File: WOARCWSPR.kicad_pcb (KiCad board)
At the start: 2 copper layers, 65 x 30.5 mm, 27 parts, among them J1 TP2, J2 Raspberry_Pi_2_3, J3 TP2, J4 Conn_Coaxial, J5 LPF_OUT, J6 LPF_IN, J7 TP1, J8 TP2, Q1 BS170, SW1 SW_Push_Dual

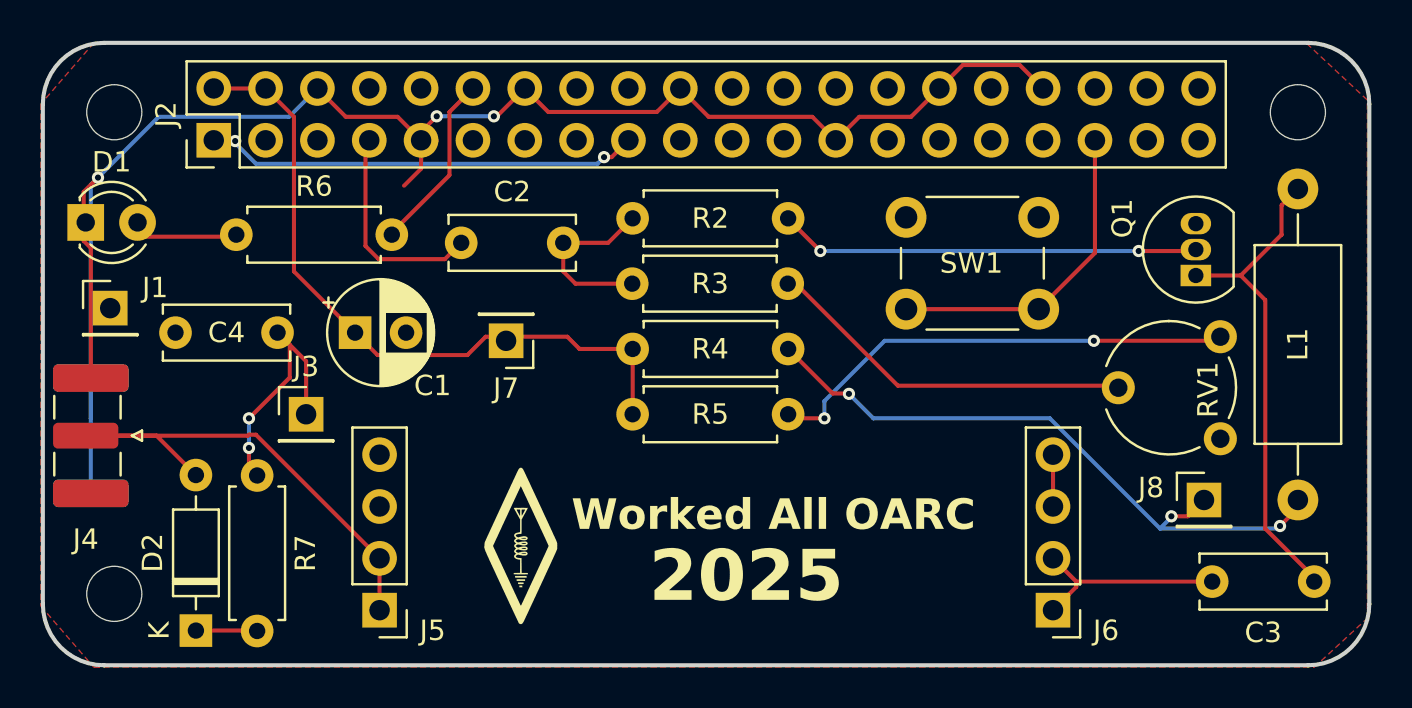
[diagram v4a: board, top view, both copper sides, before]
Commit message: Make J7 routing prettier
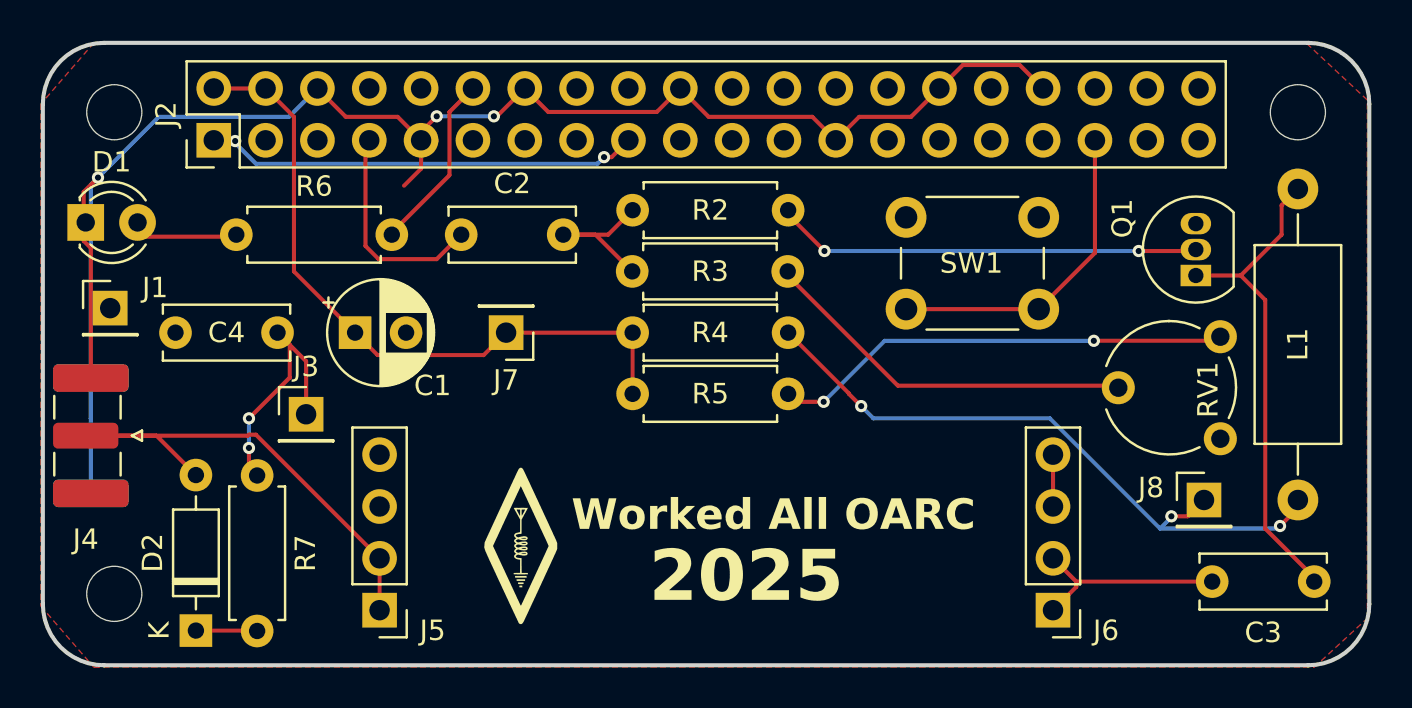
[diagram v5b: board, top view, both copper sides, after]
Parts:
- moved R5 1.00 mm to (188.4, 47.2)
- moved R4 0.80 mm to (188.4, 44.2)
- moved R3 0.60 mm to (196.0, 41.2)
- moved C2 0.40 mm to (180.0, 39.4)
- moved J7 0.40 mm to (182.2, 44.2)
- moved R2 0.40 mm to (188.4, 38.2)
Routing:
- net Net-(C2-Pad2): track 8.93 -> 8.02 mm
- net Net-(R5-Pad2): track 23.4 -> 22.7 mm
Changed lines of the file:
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@@
 	(footprint "Capacitor_THT:C_Disc_D6.0mm_W2.5mm_P5.00mm"
 		(layer "F.Cu")
-		(at 180 39.8)
+		(at 180 39.4)
 		(descr "C, Disc series, Radial, pin pitch=5.00mm, , diameter*width=6*2.5mm^2, Capacitor, http://cdn-reichelt.de/documents/datenblatt/B300/DS_KERKO_TC.pdf")
 		(tags "C Disc series Radial pin pitch 5.00mm  diameter 6mm width 2.5mm Capacitor")
@@
 	(footprint "Resistor_THT:R_Axial_DIN0207_L6.3mm_D2.5mm_P7.62mm_Horizontal"
 		(layer "F.Cu")
-		(at 188.4 38.6)
+		(at 188.4 38.2)
 		(descr "Resistor, Axial_DIN0207 series, Axial, Horizontal, pin pitch=7.62mm, 0.25W = 1/4W, length*diameter=6.3*2.5mm^2, http://cdn-reichelt.de/documents/datenblatt/B400/1_4W%23YAG.pdf")
 		(tags "Resistor Axial_DIN0207 series Axial Horizontal pin pitch 7.62mm 0.25W = 1/4W length 6.3mm diameter 2.5mm")
@@
 	(footprint "Connector_PinHeader_2.54mm:PinHeader_1x01_P2.54mm_Vertical"
 		(layer "F.Cu")
-		(at 182.2 44.6 180)
+		(at 182.2 44.2 180)
 		(descr "Through hole straight pin header, 1x01, 2.54mm pitch, single row")
 		(tags "Through hole pin header THT 1x01 2.54mm single row")
@@
 	(footprint "Resistor_THT:R_Axial_DIN0207_L6.3mm_D2.5mm_P7.62mm_Horizontal"
 		(layer "F.Cu")
-		(at 196 41.8 180)
+		(at 196 41.2 180)
 		(descr "Resistor, Axial_DIN0207 series, Axial, Horizontal, pin pitch=7.62mm, 0.25W = 1/4W, length*diameter=6.3*2.5mm^2, http://cdn-reichelt.de/documents/datenblatt/B400/1_4W%23YAG.pdf")
 		(tags "Resistor Axial_DIN0207 series Axial Horizontal pin pitch 7.62mm 0.25W = 1/4W length 6.3mm diameter 2.5mm")
@@
 	(footprint "Resistor_THT:R_Axial_DIN0207_L6.3mm_D2.5mm_P7.62mm_Horizontal"
 		(layer "F.Cu")
-		(at 188.4 45)
+		(at 188.4 44.2)
 		(descr "Resistor, Axial_DIN0207 series, Axial, Horizontal, pin pitch=7.62mm, 0.25W = 1/4W, length*diameter=6.3*2.5mm^2, http://cdn-reichelt.de/documents/datenblatt/B400/1_4W%23YAG.pdf")
 		(tags "Resistor Axial_DIN0207 series Axial Horizontal pin pitch 7.62mm 0.25W = 1/4W length 6.3mm diameter 2.5mm")
@@
 	(footprint "Resistor_THT:R_Axial_DIN0207_L6.3mm_D2.5mm_P7.62mm_Horizontal"
 		(layer "F.Cu")
-		(at 188.4 48.2)
+		(at 188.4 47.2)
 		(descr "Resistor, Axial_DIN0207 series, Axial, Horizontal, pin pitch=7.62mm, 0.25W = 1/4W, length*diameter=6.3*2.5mm^2, http://cdn-reichelt.de/documents/datenblatt/B400/1_4W%23YAG.pdf")
 		(tags "Resistor Axial_DIN0207 series Axial Horizontal pin pitch 7.62mm 0.25W = 1/4W length 6.3mm diameter 2.5mm")
@@
 	)
 	(segment
-		(start 187.2 39.8)
-		(end 188.4 38.6)
+		(start 187.2 39.4)
+		(end 185 39.4)
 		(width 0.2)
 		(layer "F.Cu")
@@
 	)
 	(segment
-		(start 185.6 41.8)
-		(end 185 41.2)
+		(start 188.38 41.2)
+		(end 186.58 39.4)
 		(width 0.2)
 		(layer "F.Cu")
@@
 	)
 	(segment
-		(start 187.2 39.8)
-		(end 185 39.8)
+		(start 188.4 38.2)
+		(end 187.2 39.4)
 		(width 0.2)
 		(layer "F.Cu")
@@
 	)
 	(segment
-		(start 185 41.2)
-		(end 185 39.8)
+		(start 186.58 39.4)
+		(end 185 39.4)
 		(width 0.2)
 		(layer "F.Cu")
@@
 	)
 	(segment
-		(start 185.6 41.8)
-		(end 188.38 41.8)
-		(width 0.2)
-		(layer "F.Cu")
-		(net 2)
-	)
-	(segment
-		(start 175.495 34.775)
-		(end 175.495 34.895)
+		(start 178.8 40.6)
+		(end 180 39.4)
 		(width 0.2)
 		(layer "F.Cu")
@@
 	)
 	(segment
-		(start 179.2 40.6)
-		(end 180 39.8)
+		(start 175.31 39.955635)
+		(end 175.954365 40.6)
 		(width 0.2)
 		(layer "F.Cu")
@@
 	)
 	(segment
-		(start 175.6 35)
-		(end 175.31 35.29)
+		(start 175.31 35.29)
+		(end 175.31 39.955635)
 		(width 0.2)
 		(layer "F.Cu")
@@
 	)
 	(segment
-		(start 175.31 35.29)
-		(end 175.31 39.955635)
+		(start 175.495 34.895)
+		(end 175.6 35)
 		(width 0.2)
 		(layer "F.Cu")
@@
 	)
 	(segment
-		(start 175.954365 40.6)
-		(end 179.2 40.6)
+		(start 175.6 35)
+		(end 175.31 35.29)
 		(width 0.2)
 		(layer "F.Cu")
@@
 	)
 	(segment
-		(start 175.31 39.955635)
-		(end 175.954365 40.6)
+		(start 175.495 34.775)
+		(end 175.495 34.895)
 		(width 0.2)
 		(layer "F.Cu")
@@
 	)
 	(segment
-		(start 175.495 34.895)
-		(end 175.6 35)
+		(start 175.954365 40.6)
+		(end 178.8 40.6)
 		(width 0.2)
 		(layer "F.Cu")
@@
 	)
 	(segment
-		(start 196.02 38.62)
-		(end 197.6 40.2)
+		(start 213.2 40.2)
+		(end 215.93 40.2)
 		(width 0.2)
 		(layer "F.Cu")
@@
 	)
 	(segment
-		(start 213.2 40.2)
-		(end 215.93 40.2)
+		(start 197.8 40.2)
+		(end 196.02 38.42)
 		(width 0.2)
 		(layer "F.Cu")
@@
 	)
 	(segment
-		(start 215.93 40.2)
-		(end 216 40.13)
+		(start 196.02 38.42)
+		(end 196.02 38.2)
 		(width 0.2)
 		(layer "F.Cu")
@@
 	)
 	(segment
-		(start 196.02 38.6)
-		(end 196.02 38.62)
+		(start 215.93 40.2)
+		(end 216 40.13)
 		(width 0.2)
 		(layer "F.Cu")
@@
 	)
 	(via
-		(at 197.6 40.2)
+		(at 197.8 40.2)
 		(size 0.6)
 		(drill 0.3)
@@
 	(segment
 		(start 213.2 40.2)
-		(end 197.6 40.2)
+		(end 197.8 40.2)
 		(width 0.2)
 		(layer "B.Cu")
@@
 	)
 	(segment
-		(start 185.2 44.4)
-		(end 185.8 45)
+		(start 188.4 44.2)
+		(end 182.2 44.2)
 		(width 0.2)
 		(layer "F.Cu")
@@
 	)
 	(segment
-		(start 181.2 44.4)
-		(end 185.2 44.4)
+		(start 175.9 45.3)
+		(end 181.1 45.3)
 		(width 0.2)
 		(layer "F.Cu")
@@
 	)
 	(segment
-		(start 175.9 45.3)
-		(end 174.8 44.2)
+		(start 174.8 44.2)
+		(end 175.9 45.3)
 		(width 0.2)
 		(layer "F.Cu")
@@
 	)
 	(segment
-		(start 181.2 44.4)
-		(end 180.3 45.3)
+		(start 188.4 47.2)
+		(end 188.4 44.2)
 		(width 0.2)
 		(layer "F.Cu")
@@
 	)
 	(segment
-		(start 185.8 45)
-		(end 188.4 45)
-		(width 0.2)
-		(layer "F.Cu")
-		(net 37)
-	)
-	(segment
-		(start 188.4 48.2)
-		(end 188.4 45)
-		(width 0.2)
-		(layer "F.Cu")
-		(net 37)
-	)
-	(segment
-		(start 180.3 45.3)
-		(end 175.9 45.3)
+		(start 181.1 45.3)
+		(end 182.2 44.2)
 		(width 0.2)
 		(layer "F.Cu")
@@
 	)
 	(segment
-		(start 199 47.2)
-		(end 198.979999 47.179999)
+		(start 198.999999 47.179999)
+		(end 196.02 44.2)
 		(width 0.2)
 		(layer "F.Cu")
@@
 	)
 	(segment
-		(start 198.979999 47.179999)
-		(end 198.199999 47.179999)
+		(start 215.6 53.2)
+		(end 216.4 52.4)
 		(width 0.2)
 		(layer "F.Cu")
@@
 	)
 	(segment
-		(start 215.6 53.2)
-		(end 216.4 52.4)
+		(start 221 52.8)
+		(end 221 52.4)
 		(width 0.2)
 		(layer "F.Cu")
@@
 	)
 	(segment
-		(start 221 52.8)
-		(end 221 52.4)
+		(start 198.999999 47.199999)
+		(end 198.999999 47.179999)
 		(width 0.2)
 		(layer "F.Cu")
@@
 	)
 	(segment
-		(start 198.199999 47.179999)
-		(end 196.02 45)
+		(start 220.124265 53.675735)
+		(end 221 52.8)
 		(width 0.2)
 		(layer "F.Cu")
@@
 	)
 	(segment
-		(start 220.124265 53.675735)
-		(end 221 52.8)
+		(start 199.6 47.8)
+		(end 198.999999 47.199999)
 		(width 0.2)
 		(layer "F.Cu")
@@
 	)
 	(via
-		(at 199 47.2)
+		(at 199.6 47.8)
 		(size 0.6)
 		(drill 0.3)
@@
 	)
 	(segment
-		(start 199 47.2)
+		(start 199.6 47.8)
 		(end 200.2 48.4)
 		(width 0.2)
@@
 	)
 	(segment
-		(start 200.2 48.4)
-		(end 208.846346 48.4)
+		(start 208.846346 48.4)
+		(end 214.246346 53.8)
 		(width 0.2)
 		(layer "B.Cu")
@@
 	)
 	(segment
-		(start 208.846346 48.4)
-		(end 214.246346 53.8)
+		(start 200.2 48.4)
+		(end 208.846346 48.4)
 		(width 0.2)
 		(layer "B.Cu")
@@
 	)
 	(segment
-		(start 196.4 41.8)
-		(end 201.4 46.8)
+		(start 212.1 46.8)
+		(end 212.2 46.9)
 		(width 0.2)
 		(layer "F.Cu")
@@
 	)
 	(segment
-		(start 201.4 46.8)
-		(end 212.1 46.8)
+		(start 196 41.4)
+		(end 201.4 46.8)
 		(width 0.2)
 		(layer "F.Cu")
@@
 	)
 	(segment
-		(start 196 41.8)
-		(end 196.4 41.8)
+		(start 201.4 46.8)
+		(end 212.1 46.8)
 		(width 0.2)
 		(layer "F.Cu")
@@
 	)
 	(segment
-		(start 212.1 46.8)
-		(end 212.2 46.9)
+		(start 196 41.2)
+		(end 196 41.4)
 		(width 0.2)
 		(layer "F.Cu")
@@
 	)
 	(segment
-		(start 196.02 48.2)
-		(end 196.22 48.4)
+		(start 217 44.6)
+		(end 217.2 44.4)
 		(width 0.2)
 		(layer "F.Cu")
@@
 	)
 	(segment
-		(start 217 44.6)
-		(end 217.2 44.4)
+		(start 197.761471 47.59)
+		(end 196.41 47.59)
 		(width 0.2)
 		(layer "F.Cu")
@@
 	)
 	(segment
-		(start 196.22 48.4)
-		(end 197.8 48.4)
+		(start 196.41 47.59)
+		(end 196.02 47.2)
 		(width 0.2)
 		(layer "F.Cu")
@@
 	)
 	(via
-		(at 197.8 48.4)
+		(at 197.761471 47.59)
 		(size 0.6)
 		(drill 0.3)
@@
 	)
 	(segment
-		(start 197.8 48.4)
-		(end 197.8 47.551471)
-		(width 0.2)
-		(layer "B.Cu")
-		(net 41)
-	)
-	(segment
-		(start 197.8 47.551471)
+		(start 197.761471 47.59)
 		(end 200.751471 44.6)
 		(width 0.2)

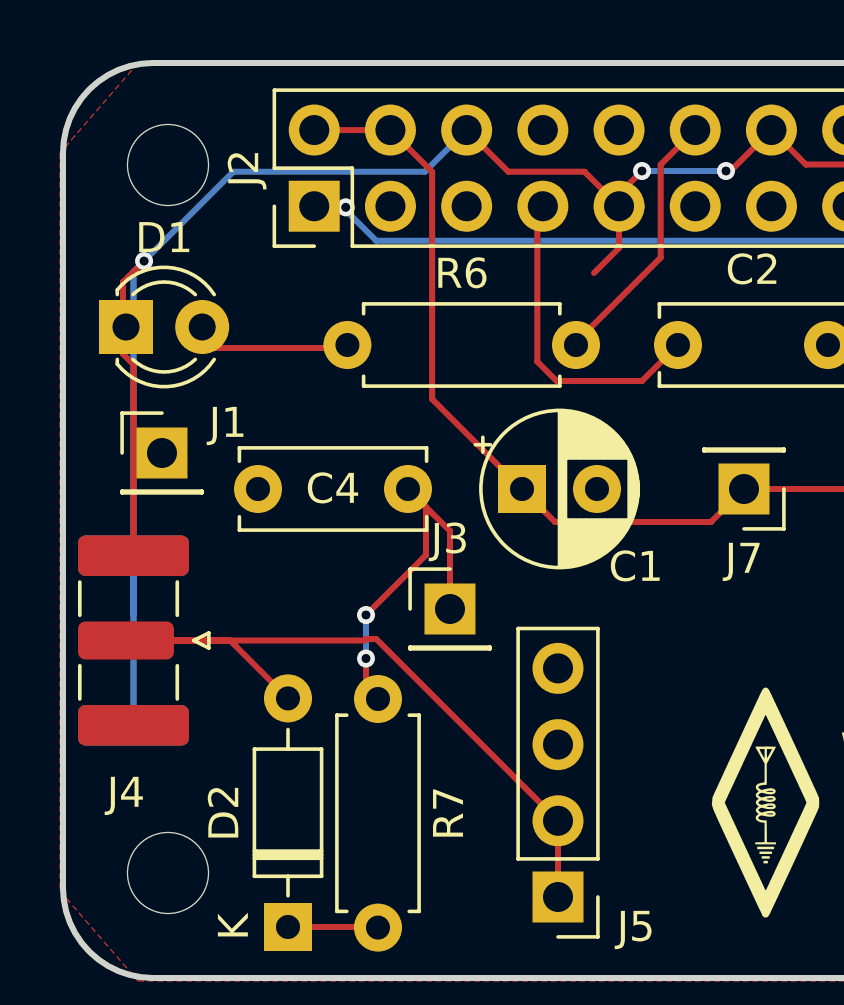
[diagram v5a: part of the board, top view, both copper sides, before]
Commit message: Update SMA footprint for correct size of connector
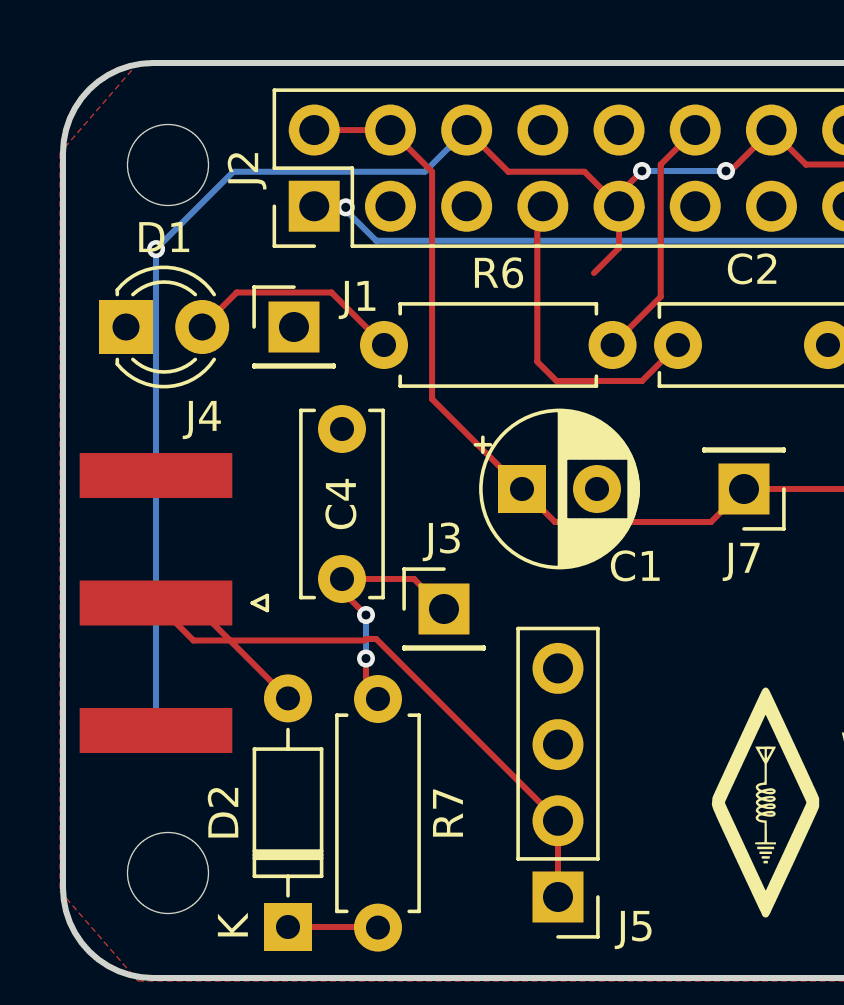
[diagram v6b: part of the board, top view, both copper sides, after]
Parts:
- J4: footprint Connector_Coaxial:SMA_Samtec_SMA-J-P-H-ST-EM1_EdgeMount -> Connector_Coaxial:SMA_Amphenol_132289_EdgeMount
- moved J1 6.08 mm to (167.2, 38.8)
- moved C4 3.44 mm to (168.8, 42.2), turned to -90 degrees
- moved J4 1.60 mm to (162.6, 48.0)
- moved R6 1.22 mm to (170.2, 39.4)
- moved J3 0.20 mm to (172.2, 48.2)
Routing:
- net GND: track 88.5 -> 76.2 mm
- net Net-(J3-Pin_1): track 12.8 -> 8.31 mm
- net Net-(D1-A): track 4.31 -> 7.26 mm
- net Net-(D2-A): track 25.9 -> 25.0 mm
- net Net-(J2-GPIO18/PWM0): track 8.99 -> 8.31 mm
